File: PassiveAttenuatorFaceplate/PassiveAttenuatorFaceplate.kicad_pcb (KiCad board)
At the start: 2 copper layers, 15 x 128.5 mm, 8 parts

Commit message: Update to kicad 10 Change logo on faceplate Change faceplate jack graphics to round from square Regenerate gerbers
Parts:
- added G***: LOGO, _NTSFootprints:SchentronicsLogoSsmall, F.Cu at (144.5, 149.5)
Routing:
- added copper zone on F.Cu, net (none)
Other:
- net class Default removed
- board text removed: "Schenk"

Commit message: Faceplate: S-mark + new ST-02 on the hole-centered scheme, Orbitron text
S-mark moves from lower-left to the gap right of the bottom hole
(1.09mm margin each side) -- too narrow for the full wordmark, so this
is the small-mark branch of the placement rule. Adds ST-02, which didn't
exist before, vertical, justify-left anchored to the S-mark's bottom in
the left gap. Header ("Atten.") switched from italic KiCad stroke font
to upright Orbitron.
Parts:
- moved G*** 10.7 mm to (155.2, 148.8)
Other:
- board text added: "ST-02"
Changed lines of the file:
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@@
 	(footprint "_NTSFootprints:SchentronicsLogoSsmall"
 		(layer "F.Cu")
-		(at 144.5 149.5)
+		(at 155.2079 148.7500)
 		(property "Reference" "G***"
 			(at 0 0 0)
@@
 		(effects
 			(font
+				(face "Orbitron")
 				(size 2.5 2.5)
 				(thickness 0.4)
-				(italic yes)
-			)
-		)
-	)
+			)
+		)
+	)
+	(gr_text "ST-02"
+		(at 144.7500 149.9597 90)
+		(layer "F.SilkS")
+		(effects
+			(font
+				(face "Orbitron")
+				(size 1.7 1.7)
+				(thickness 0.3)
+			)
+			(justify left)
+		)
+	)

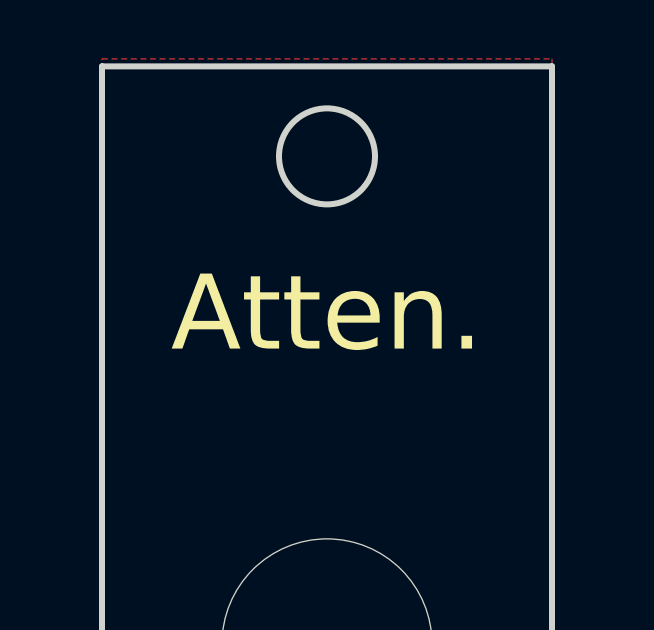
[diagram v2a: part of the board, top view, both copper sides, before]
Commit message: Faceplate: rename header "Atten." to "Attenuate", narrow to fit 15mm width
Width dropped from 2.5mm to 2mm (height unchanged at 2.5mm) to get the
longer name under the 3 HP panel's width. Also carries KiCad's own
render_cache entries for the Orbitron text, written on save -- confirms
the font is rendering correctly, not falling back.
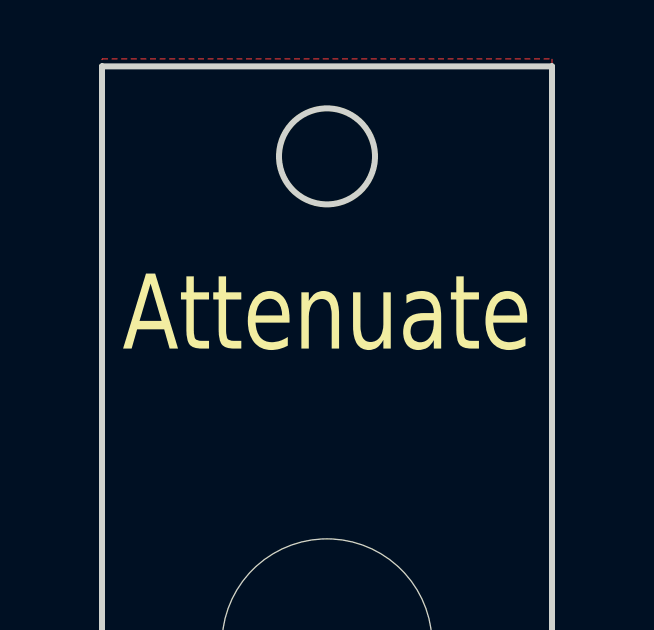
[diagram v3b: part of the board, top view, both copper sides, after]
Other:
- board text added: "Attenuate"
- board text removed: "Atten."
